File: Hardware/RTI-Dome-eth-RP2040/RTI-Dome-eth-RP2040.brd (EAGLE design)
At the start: 111.1 x 76.3 mm, 104 parts, among them IC2 24LC128T-I_SN, IC3 FT232RL, IC4 RASPBERRY_PI_PICO, IC5 74LVC245, IC6 74ABT245, IC8 REG1117-3.3V, IC9 REG1117-5V, J2 XT60PW-M, U1 W5500, X13 PN61729-S, X9 J1011F21PNL

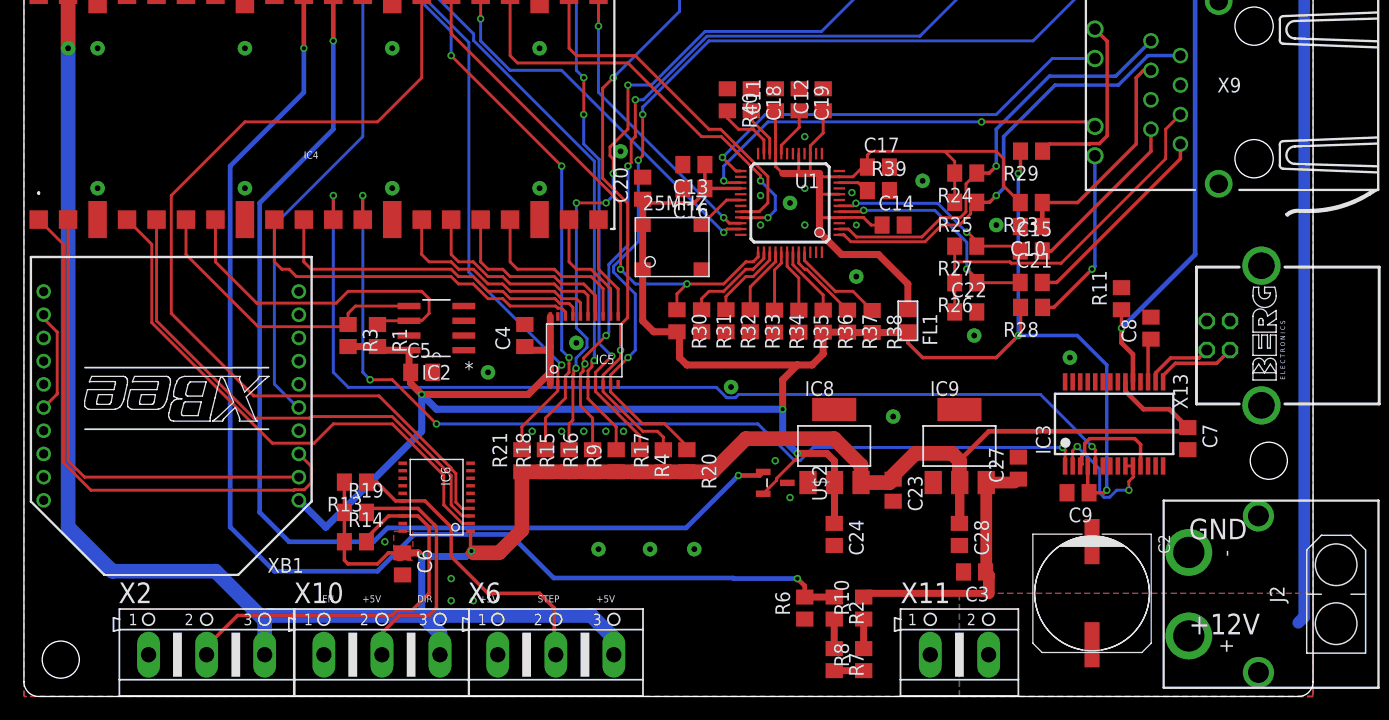
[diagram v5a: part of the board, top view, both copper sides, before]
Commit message: Fix some component labels
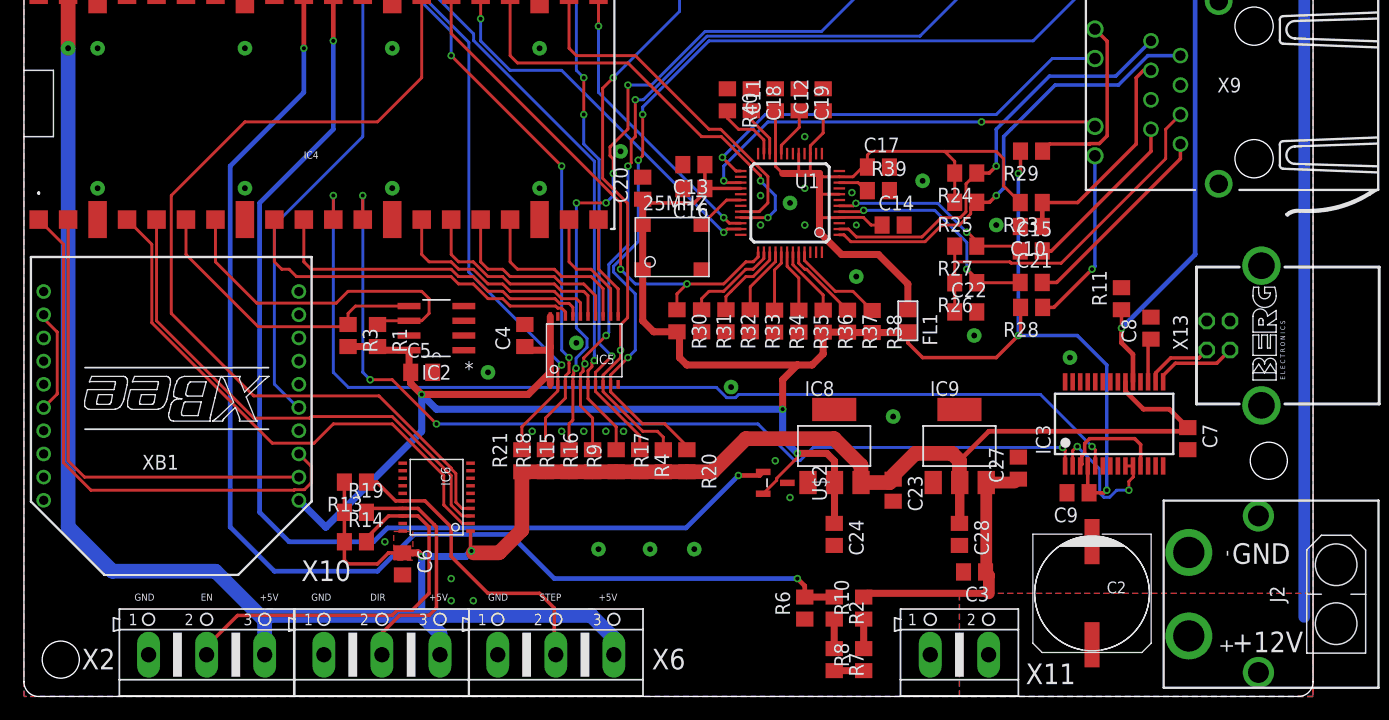
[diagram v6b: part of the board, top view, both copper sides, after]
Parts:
- IC4: device samacsys:RASPBERRYPIPICOW -> samacsys:RASPBERRYPIPICO
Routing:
- net +12V: track 154.7 -> 154.0 mm

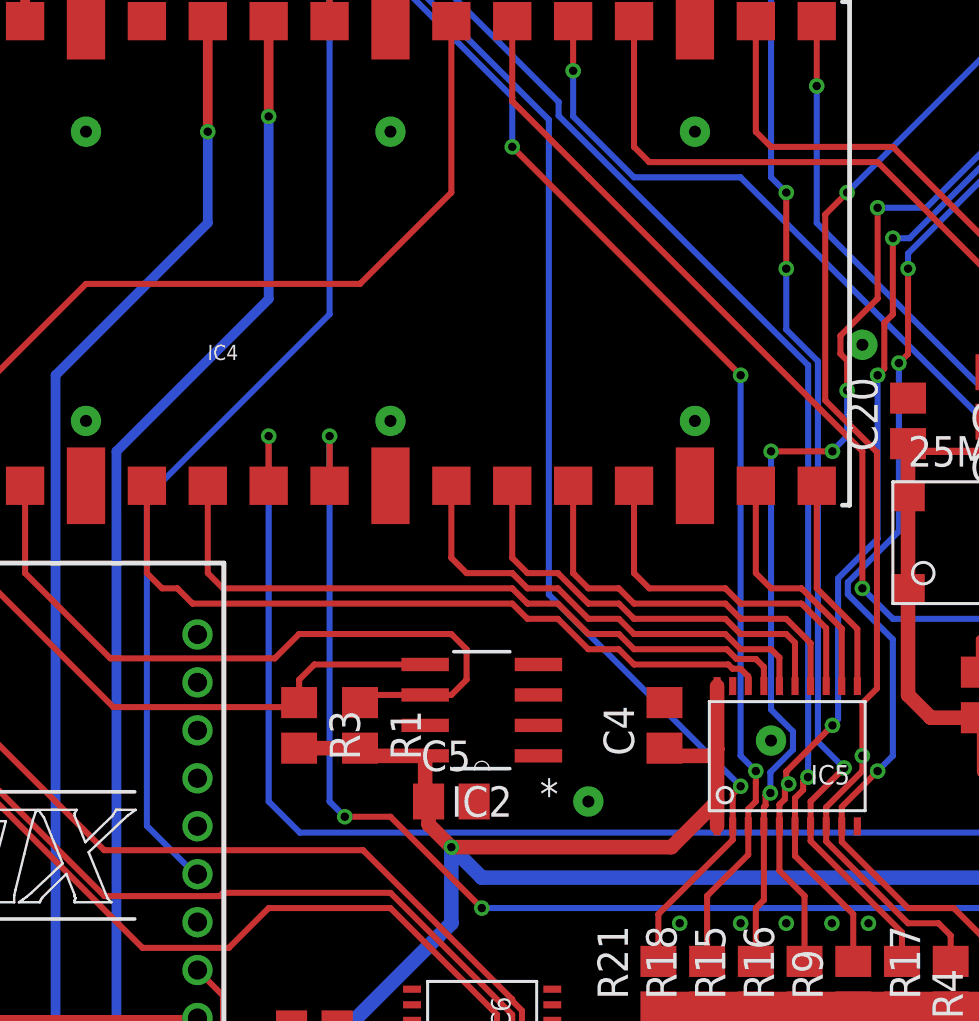
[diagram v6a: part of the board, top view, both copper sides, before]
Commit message: Track cleanup on RP-2040 board
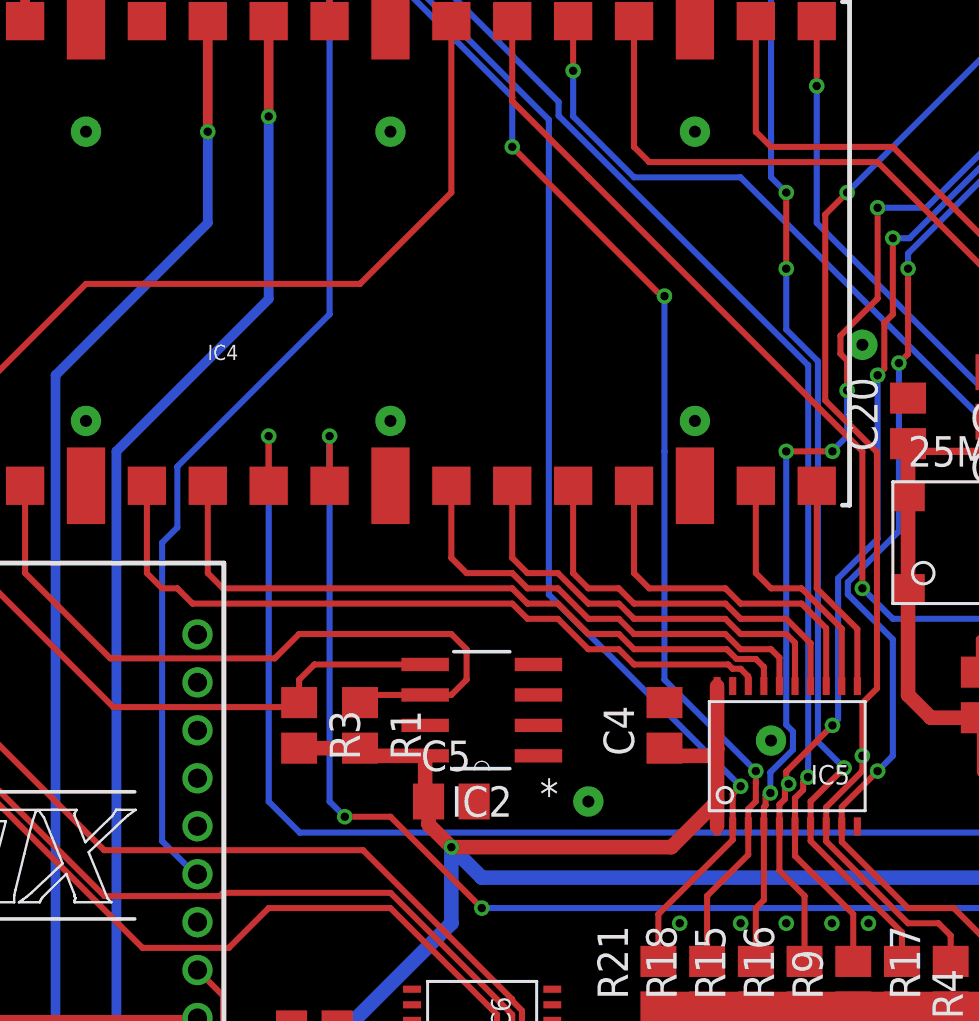
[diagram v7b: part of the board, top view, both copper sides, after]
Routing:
- net BUTTON_WEST_CLOSE_IN_5V: track 67.1 -> 66.2 mm
- net XBEE_RESET: track 43.1 -> 42.6 mm
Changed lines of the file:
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@@
 <via x="29.21" y="62.23" extent="1-16" drill="0.35"/>
 <wire x1="29.21" y1="62.23" x2="29.21" y2="48.26" width="0.254" layer="16"/>
-<wire x1="29.21" y1="48.26" x2="21.59" y2="40.64" width="0.254" layer="16"/>
-<wire x1="21.59" y1="40.64" x2="21.59" y2="26.924" width="0.254" layer="16"/>
-<wire x1="21.59" y1="26.924" x2="23.606" y2="24.908" width="0.254" layer="16"/>
-<wire x1="23.606" y1="24.908" x2="23.7" y2="24.908" width="0.254" layer="16"/>
+<wire x1="22.86" y1="41.91" x2="29.21" y2="48.26" width="0.254" layer="16"/>
+<wire x1="23.7" y1="24.908" x2="23.606" y2="24.908" width="0.254" layer="16"/>
+<wire x1="22.225" y1="38.735" x2="22.86" y2="39.37" width="0.254" layer="16"/>
+<wire x1="22.86" y1="39.37" x2="22.86" y2="41.91" width="0.254" layer="16"/>
+<wire x1="23.606" y1="24.908" x2="22.225" y2="26.289" width="0.254" layer="16"/>
+<wire x1="22.225" y1="26.289" x2="22.225" y2="38.735" width="0.254" layer="16"/>
 </signal>
 <signal name="N$9">
@@
 <wire x1="56.35995" y1="63.8782" x2="32.6003125" y2="63.8782" width="0.254" layer="16"/>
 <via x="36.83" y="55.245" extent="1-16" drill="0.35"/>
-<wire x1="36.83" y1="55.245" x2="46.355" y2="45.72" width="0.254" layer="1"/>
-<via x="46.355" y="45.72" extent="1-16" drill="0.35"/>
-<wire x1="46.355" y1="45.72" x2="46.355" y2="29.845" width="0.254" layer="16"/>
-<wire x1="46.355" y1="29.845" x2="46.99" y2="29.21" width="0.254" layer="16"/>
+<wire x1="36.83" y1="55.245" x2="43.108703125" y2="48.966296875" width="0.254" layer="1"/>
+<wire x1="43.18" y1="49.022" x2="43.108703125" y2="48.966296875" width="0.254" layer="1"/>
+<via x="43.18" y="49.022" extent="1-16" drill="0.35"/>
+<wire x1="43.18" y1="49.022" x2="43.18" y2="42.545" width="0.254" layer="16"/>
+<wire x1="43.18" y1="42.545" x2="43.18" y2="33.02" width="0.254" layer="16"/>
+<wire x1="43.18" y1="33.02" x2="46.99" y2="29.21" width="0.254" layer="16"/>
 </signal>
 <signal name="BUTTON_WEST_CLOSE_IN_5V">
@@
 <wire x1="47.5968" y1="28.29424375" x2="47.5968" y2="29.1586375" width="0.254" layer="16"/>
 <wire x1="47.5968" y1="29.1586375" x2="48.5394" y2="30.1012375" width="0.254" layer="16"/>
-<wire x1="48.5394" y1="30.8587625" x2="47.625" y2="31.7731625" width="0.254" layer="16"/>
-<wire x1="47.625" y1="31.7731625" x2="47.625" y2="42.545" width="0.254" layer="16"/>
-<via x="47.625" y="42.545" extent="1-16" drill="0.35"/>
+<wire x1="48.5394" y1="30.8587625" x2="48.26" y2="31.1381625" width="0.254" layer="16"/>
+<wire x1="48.26" y1="42.545" x2="48.26" y2="31.1381625" width="0.254" layer="16"/>
+<via x="48.26" y="42.545" extent="1-16" drill="0.35"/>
 <wire x1="50.5206" y1="47.3687625" x2="50.5206" y2="46.6112375" width="0.254" layer="1"/>
 <wire x1="52.07" y1="52.705" x2="52.07" y2="48.9181625" width="0.254" layer="1"/>
@@
 <wire x1="50.165" y1="42.545" x2="50.1876" y2="42.545" width="0.254" layer="16"/>
 <via x="50.1876" y="42.545" extent="1-16" drill="0.35"/>
-<wire x1="50.1876" y1="42.545" x2="47.625" y2="42.545" width="0.254" layer="1"/>
+<wire x1="50.1876" y1="42.545" x2="48.26" y2="42.545" width="0.254" layer="1"/>
 </signal>
 <signal name="HOME_SHUTTER_CLOSED-IN_EXT">
